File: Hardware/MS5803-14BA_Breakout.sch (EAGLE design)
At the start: 18 parts, among them U1 MS5803-14BA

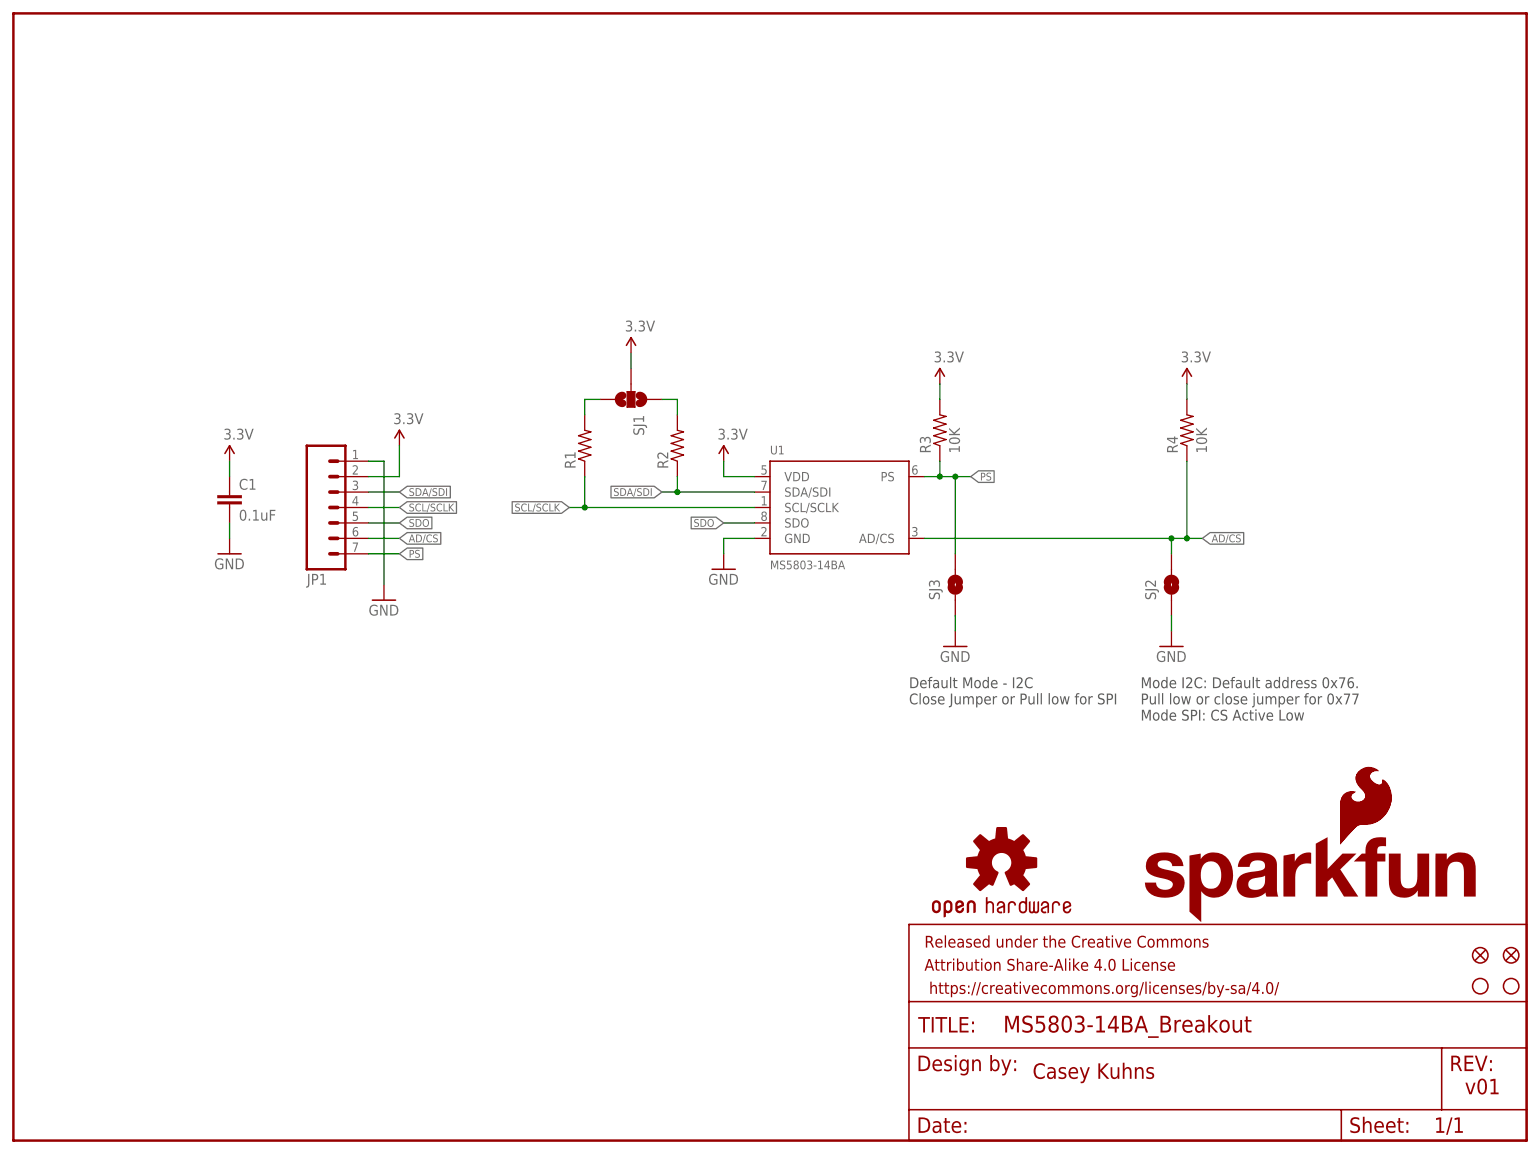
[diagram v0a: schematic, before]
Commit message: changed I2C resistors to 2.2k, updated rev numbers, Moved to new jumper package
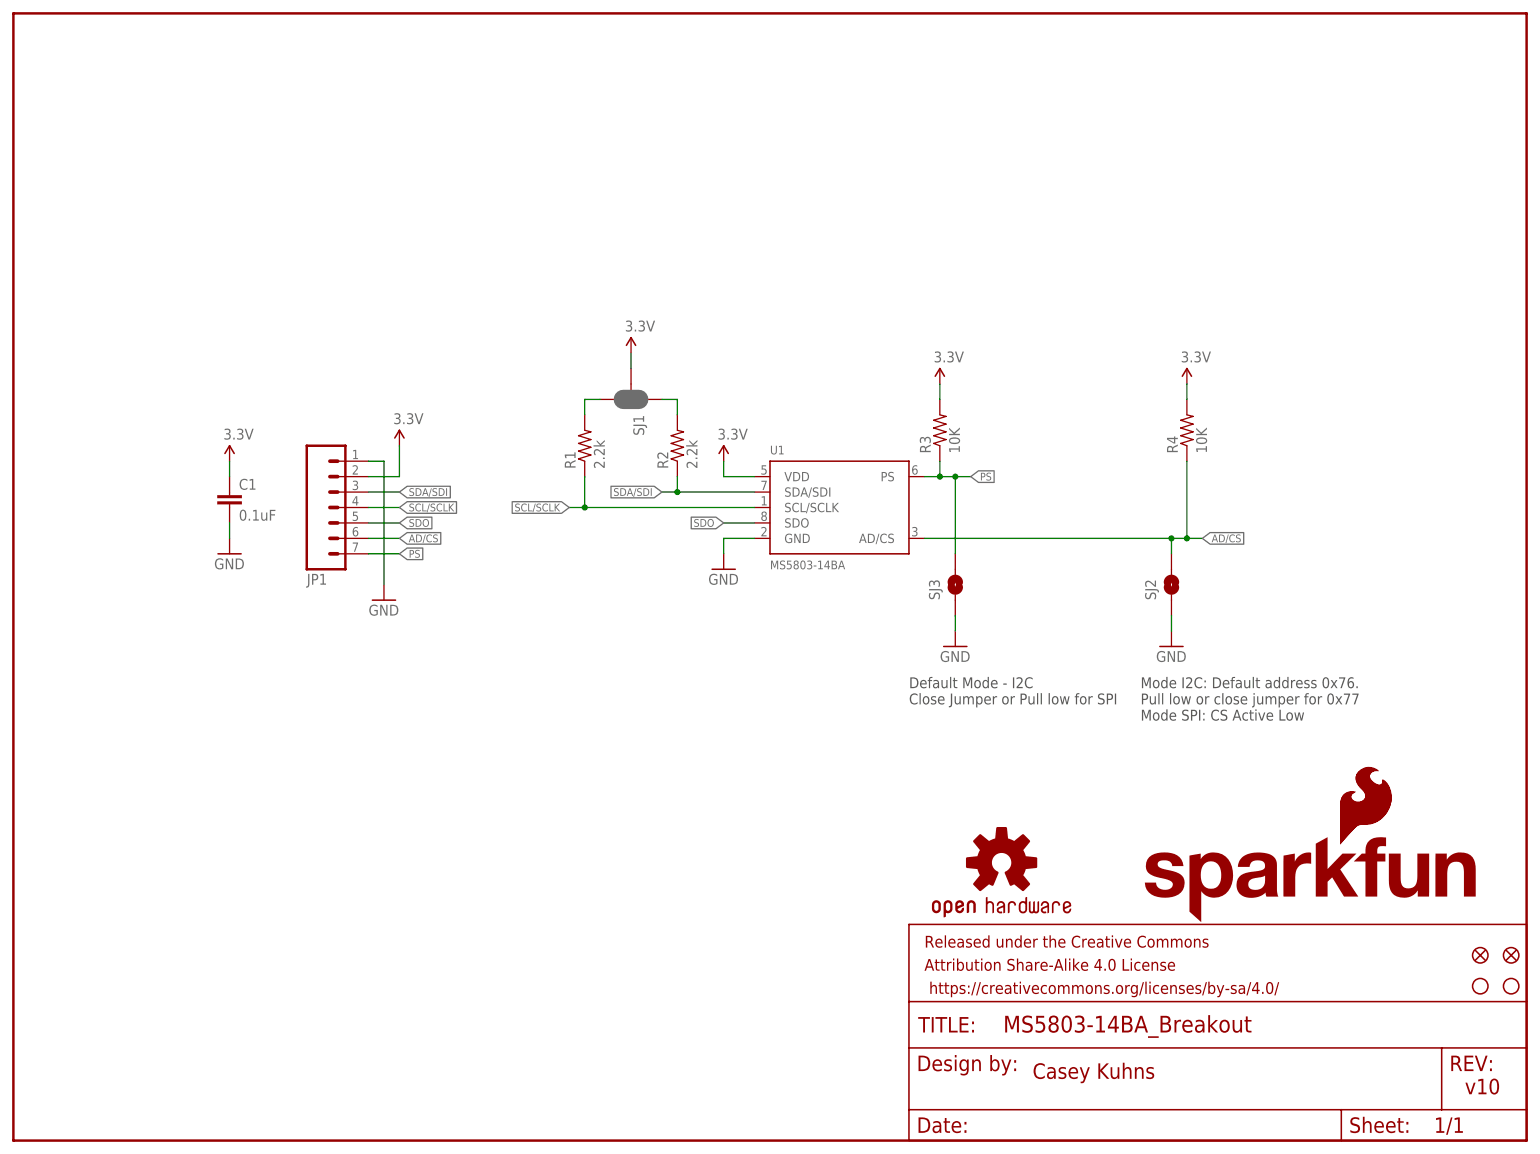
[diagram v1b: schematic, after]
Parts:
- R1, R2: value (none) -> 2.2k; device SparkFun-Resistors:4.7KOHM1/10W1%(0603) -> SparkFun-Resistors:2.2KOHM1/10W1%(0603)
- SJ1: value (none) -> JUMPER-PAD-3-NC_BY_PASTE; device SparkFun-Passives:SOLDERJUMPER_2WAYPASTE1&2&3 -> SparkFun-Passives:JUMPER-PAD-3-NC_BY_PASTE
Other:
- note added: "v10"
- note removed: "v01"
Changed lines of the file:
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@@
 <part name="JP1" library="SparkFun-Connectors" deviceset="M07" device=""/>
 <part name="C1" library="SparkFun-Capacitors" deviceset="0.1UF-25V(+80/-20%)(0603)" device="" value="0.1uF"/>
-<part name="R1" library="SparkFun-Resistors" deviceset="4.7KOHM1/10W1%(0603)" device=""/>
-<part name="R2" library="SparkFun-Resistors" deviceset="4.7KOHM1/10W1%(0603)" device=""/>
-<part name="SJ1" library="SparkFun-Passives" deviceset="SOLDERJUMPER_2WAY" device="PASTE1&amp;2&amp;3"/>
+<part name="R1" library="SparkFun-Resistors" deviceset="2.2KOHM1/10W1%(0603)" device="" value="2.2k"/>
+<part name="R2" library="SparkFun-Resistors" deviceset="2.2KOHM1/10W1%(0603)" device="" value="2.2k"/>
+<part name="SJ1" library="SparkFun-Passives" deviceset="JUMPER-PAD-3-NC_BY_PASTE" device="" value=""/>
 <part name="STANDOFF1" library="SparkFun-Electromechanical" deviceset="STAND-OFF" device="TIGHT"/>
 <part name="STANDOFF2" library="SparkFun-Electromechanical" deviceset="STAND-OFF" device="TIGHT"/>
@@
 <plain>
 <text x="167.64" y="10.16" size="2.54" layer="94">Casey Kuhns</text>
-<text x="238.76" y="7.62" size="2.54" layer="94">v01</text>
+<text x="238.76" y="7.62" size="2.54" layer="94">v10</text>
 <text x="147.32" y="76.2" size="1.778" layer="97" align="top-left">Default Mode - I2C
 Close Jumper or Pull low for SPI</text>
